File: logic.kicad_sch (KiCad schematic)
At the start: 4 parts, among them U1 ESP32-C3-MINI-1, U5 SPL06-001, U7 LTR-303ALS-01

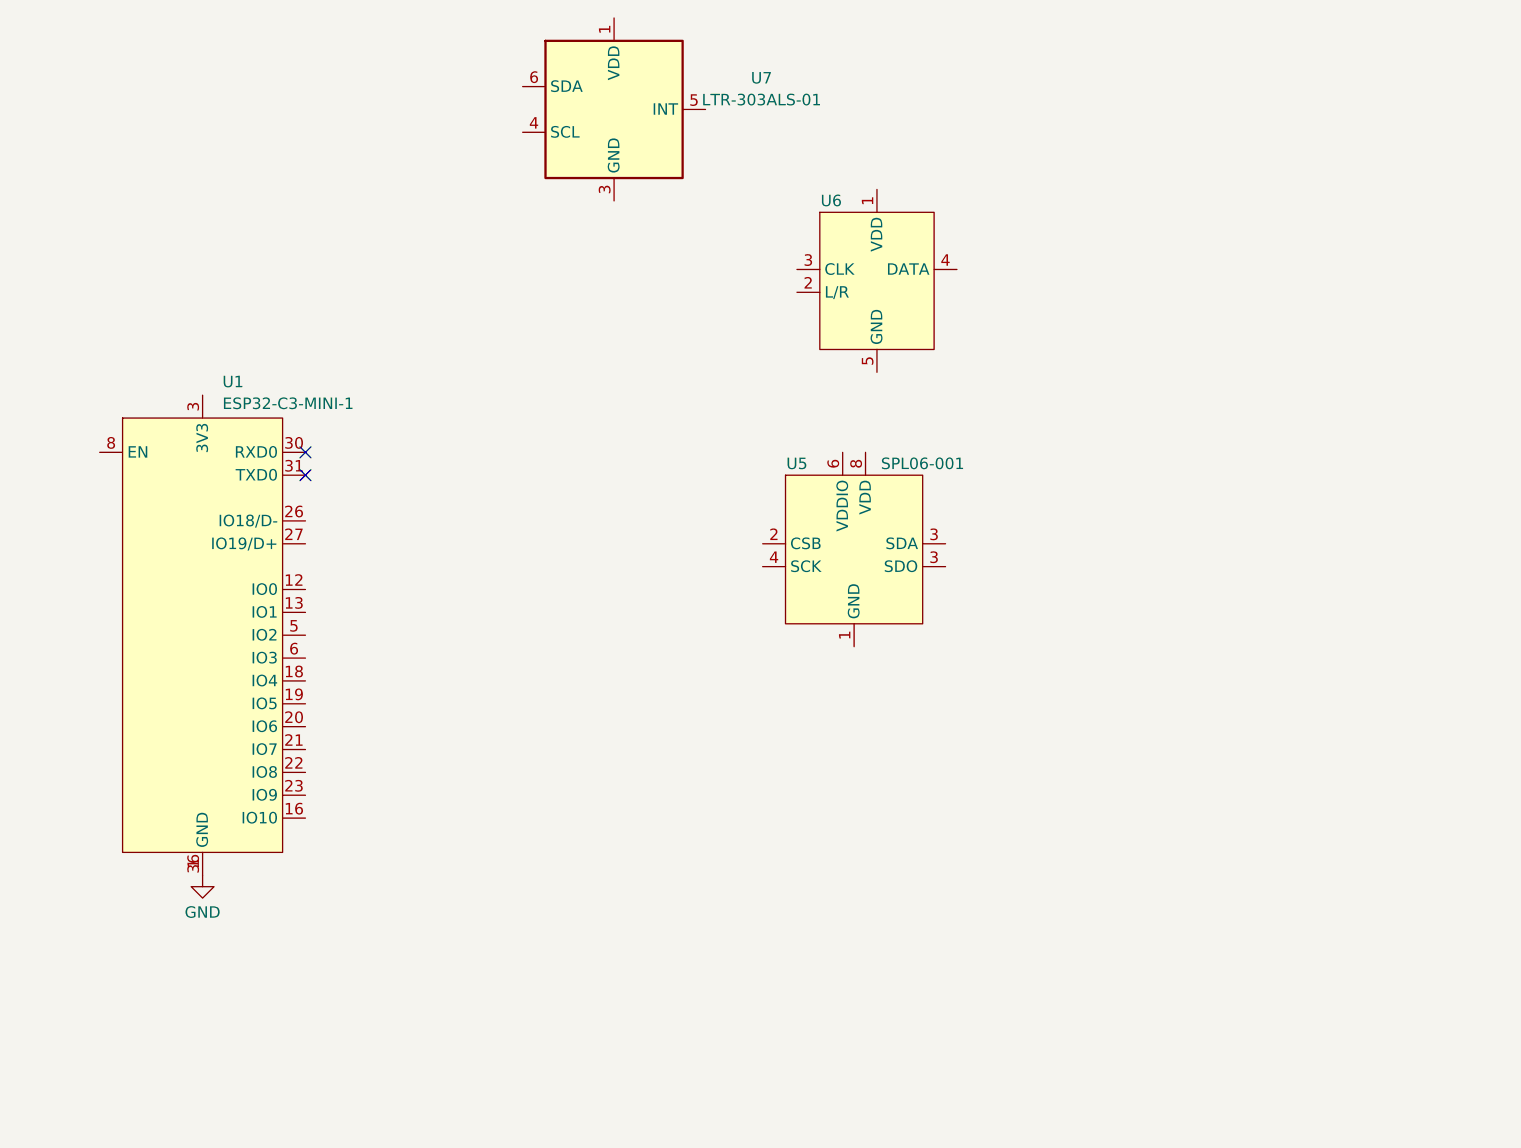
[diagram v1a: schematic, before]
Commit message: Finish preliminary charger and logic schematic
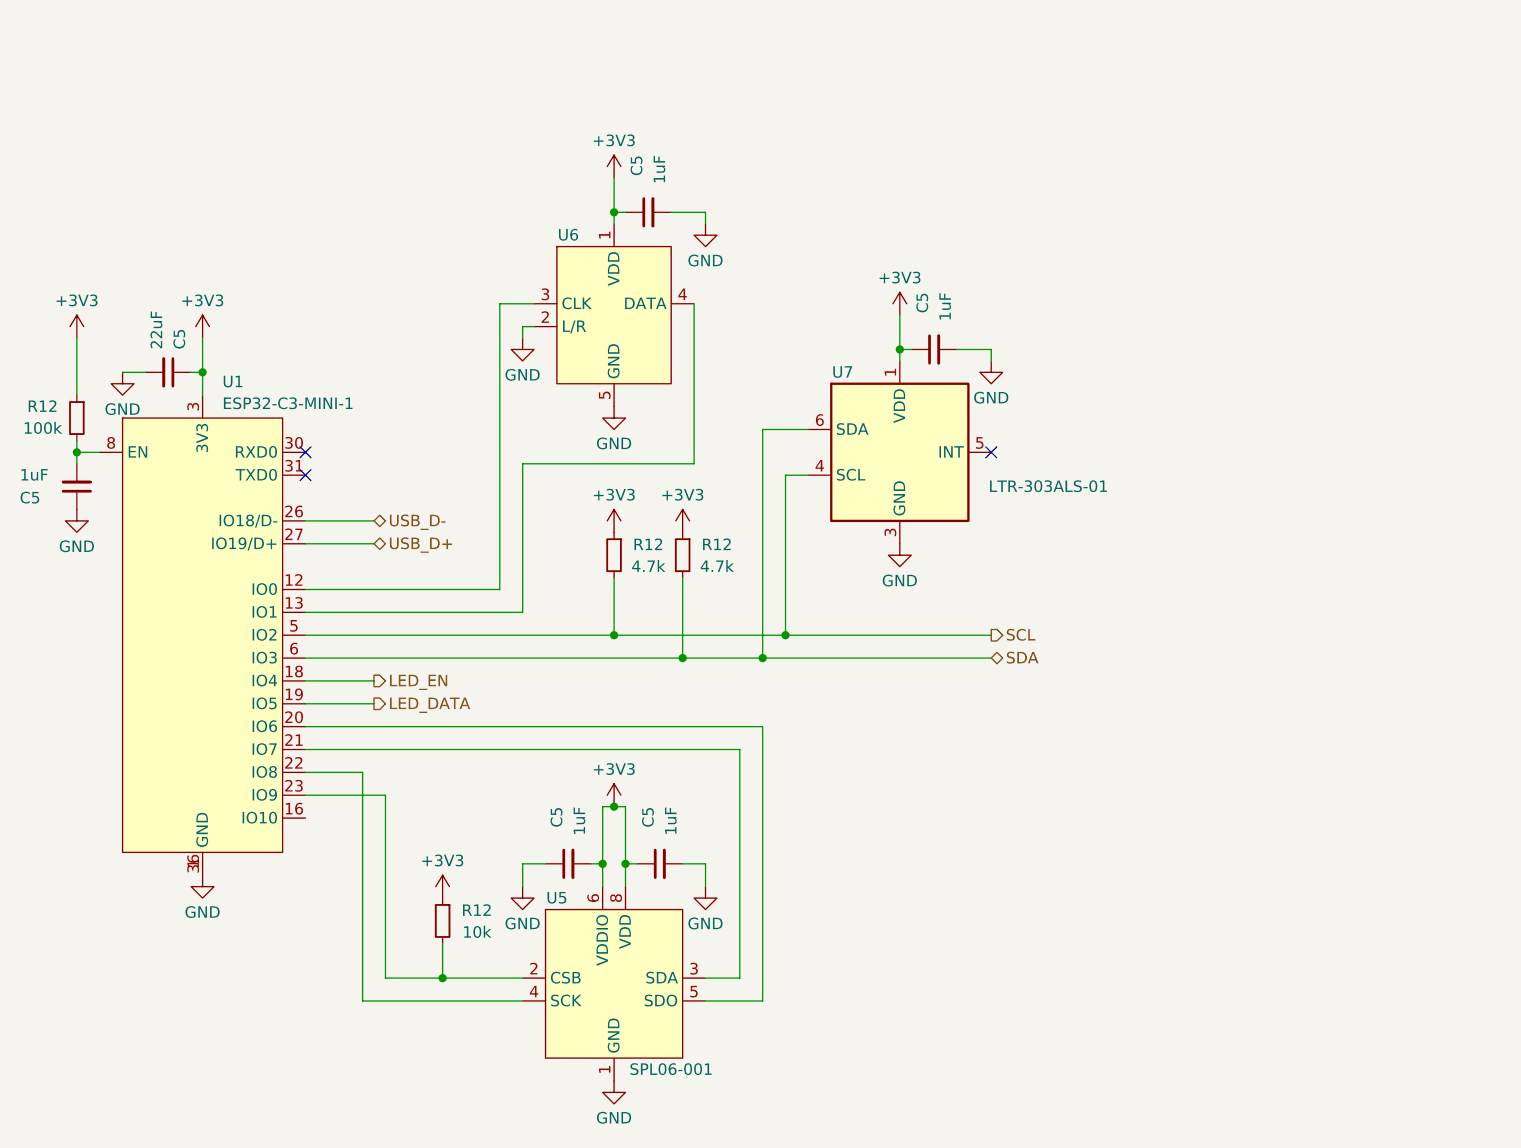
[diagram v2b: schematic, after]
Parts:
- added C5 (x5): 1uF, Capacitor_SMD:C_0402_1005Metric, symbol Device:C_Small
- added C5: 22uF, Capacitor_SMD:C_0805_2012Metric, symbol Device:C_Small
- added R12: 100k, Resistor_SMD:R_0402_1005Metric, symbol Device:R_Small
- added R12: 10k, Resistor_SMD:R_0402_1005Metric, symbol Device:R_Small
- added R12 (x2): 4.7k, Resistor_SMD:R_0402_1005Metric, symbol Device:R_Small
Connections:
- net GND: now also U6.2 (L/R), U6.5 (GND), U7.3 (GND), C5.1, C5.1, C5.2, C5.2, C5.2, C5.2
- net +3V3: now reaches U7.1 (VDD)
- net +3V3: now also U1.3 (3V3), U5.6 (VDDIO), U5.8 (VDD), U6.1 (VDD), C5.1, C5.1, C5.1, C5.1, C5.2, R12.1, R12.1, R12.1, R12.1
- net SCL: now reaches U7.4 (SCL)
- net SCL: now also U1.5 (IO2), R12.2
- net SDA: now reaches U7.6 (SDA)
- net SDA: now also U1.6 (IO3), R12.2
- net at U1.12 (IO0): now also U6.3 (CLK)
- net at U1.13 (IO1): now also U6.4 (DATA)
- net LED_EN: now reaches U1.18 (IO4)
- net LED_DATA: now reaches U1.19 (IO5)
- net at U1.20 (IO6): now also U5.5 (SDO)
- net at U1.21 (IO7): now also U5.3 (SDA)
- net at U1.22 (IO8): now also U5.4 (SCK)
- net at U1.23 (IO9): now also U5.2 (CSB), R12.2
- net USB_D-: now reaches U1.26 (IO18/D-)
- net USB_D+: now reaches U1.27 (IO19/D+)
- net at U1.8 (EN): now also C5.2, R12.2
- no-connect marks 2 -> 3
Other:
- moved on the sheet: U5, U6, U7

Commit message: Finish rough layout
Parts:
- added R12 (x2): 330, Resistor_SMD:R_0402_1005Metric, symbol Device:R_Small
- added R12: 10k, Resistor_SMD:R_0402_1005Metric, symbol Device:R_Small
- C5: value 22uF -> 10uF; footprint Capacitor_SMD:C_0805_2012Metric -> Capacitor_SMD:C_0402_1005Metric; LCSC C45783 -> C15525
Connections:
- net LED_EN is gone; now on an unnamed net: U1.18 (IO4)
- net LED_DATA: now also U1.6 (IO3); no longer U1.19 (IO5)
- net SDA: now also U1.12 (IO0); no longer U1.6 (IO3)
- net at U6.3 (CLK): now also U1.19 (IO5); no longer U1.12 (IO0)
- net at U6.4 (DATA): no longer U1.13 (IO1)
- net at U1.16 (IO10): now also R12.2
- net at U1.30 (RXD0): now also R12.2
- net at U1.31 (TXD0): now also R12.2
- new net CHRG_EN: U1.13 (IO1)
- new net LED1: R12.1
- new net LED2: R12.1
- new net PWR_ON: R12.1
- no-connect marks 3 -> 1
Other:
- moved on the sheet: C5, R12, U5

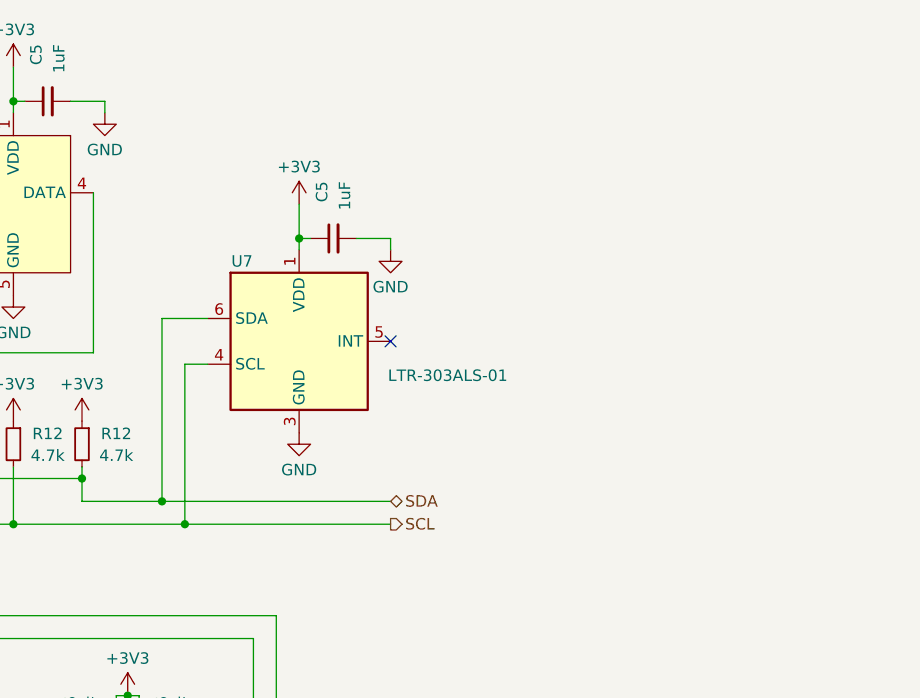
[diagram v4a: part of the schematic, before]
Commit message: Add accelerometer
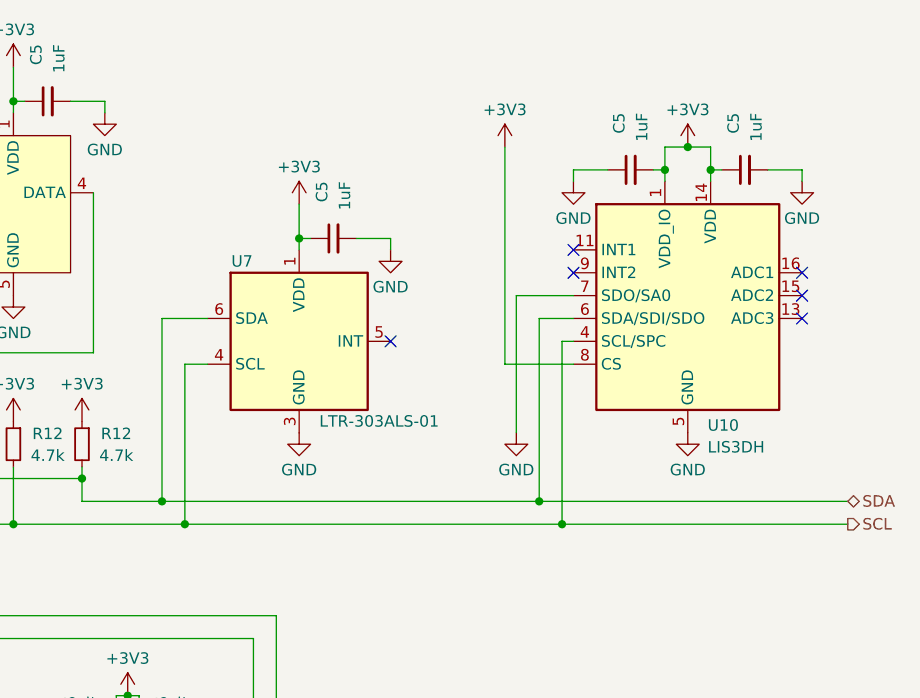
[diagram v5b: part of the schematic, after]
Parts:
- added C5 (x2): 1uF, Capacitor_SMD:C_0402_1005Metric, symbol Device:C_Small
- added U10: LIS3DH, Package_LGA:LGA-16_3x3mm_P0.5mm_LayoutBorder3x5y, symbol Sensor_Motion:LIS3DH
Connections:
- net +3V3: now also C5.1, C5.2, U10.1 (VDD_IO), U10.14 (VDD), U10.8 (CS)
- net GND: now also C5.1, C5.2, U10.10 (GND), U10.12 (GND), U10.5 (GND), U10.7 (SDO/SA0)
- net SCL: now also U10.4 (SCL/SPC)
- net SDA: now also U10.6 (SDA/SDI/SDO)
- no-connect marks 1 -> 6
